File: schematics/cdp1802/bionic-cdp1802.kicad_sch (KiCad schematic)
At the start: 5 parts, among them J1 Bionic-P135, J2 Bionic-P245, U1 CDP1802, U2 74HCT126

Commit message: [CDP1802] Move schematics directory
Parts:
- added U3: 11AA010-I/TO, TO-92_MC_MCH, symbol 0-LocalLibrary:11AA010-I_TO
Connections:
- net GND: now also U3.1 (VSS)
- net VCC: now also U3.3 (VCC)
- net at J2.26 (P57): now also U3.2 (SCIO)
- no-connect marks 9 -> 8
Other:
- title: BionicCDP1802 Mezzanine -> BionicCDP1802

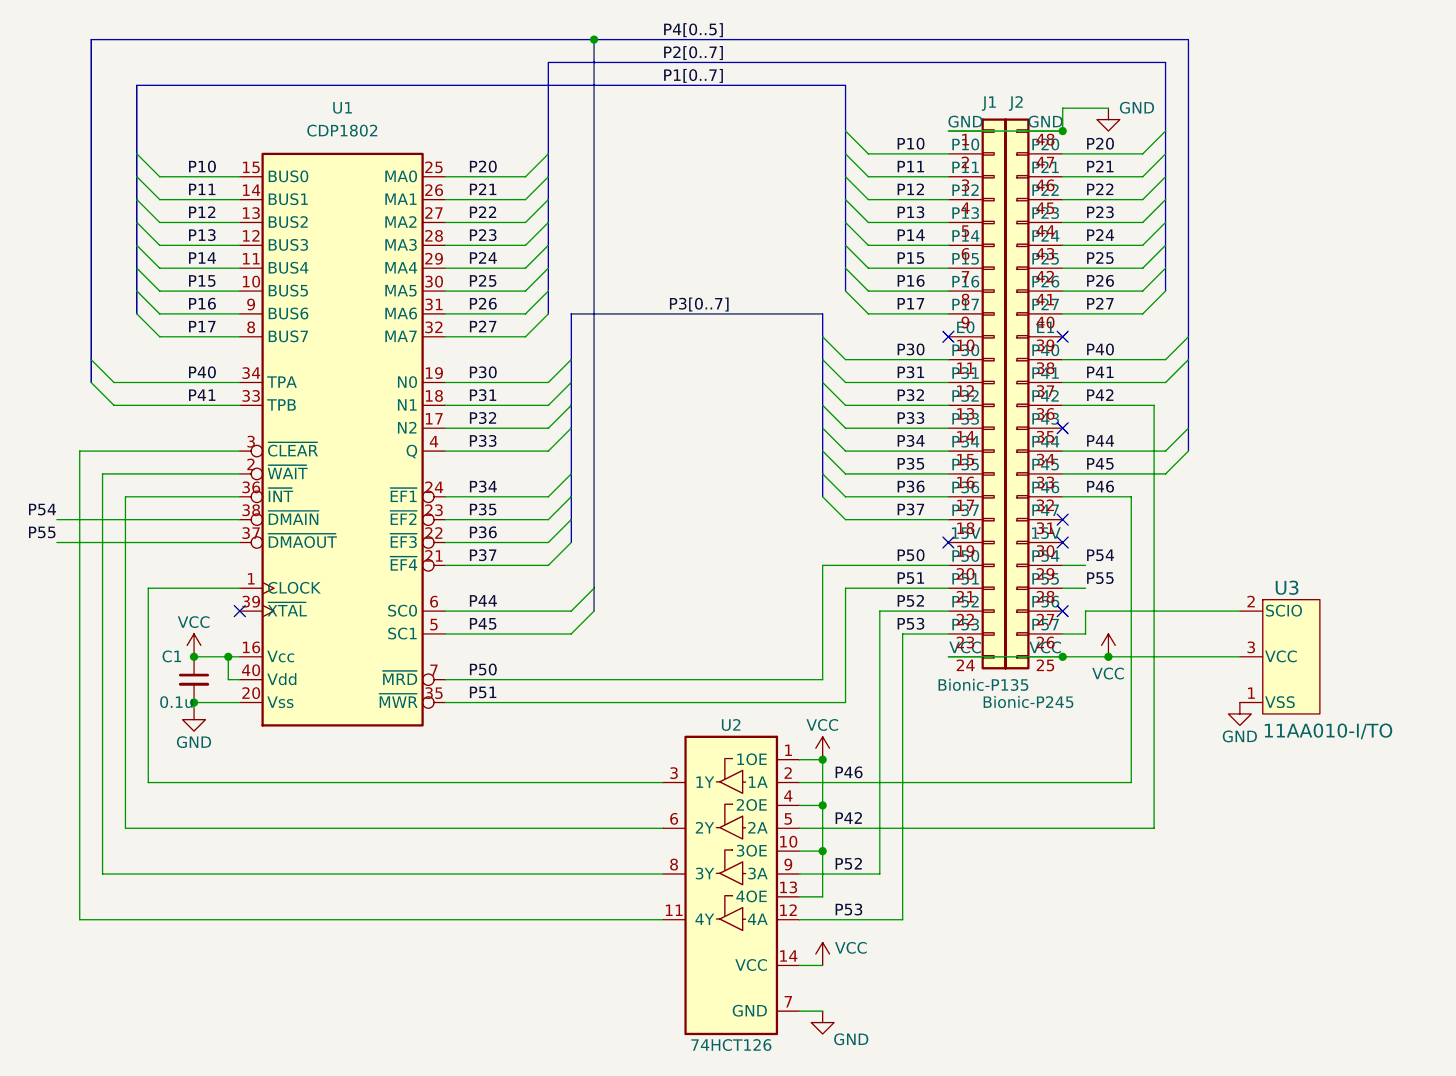
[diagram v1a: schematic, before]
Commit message: [CDP1802] Remove HC126
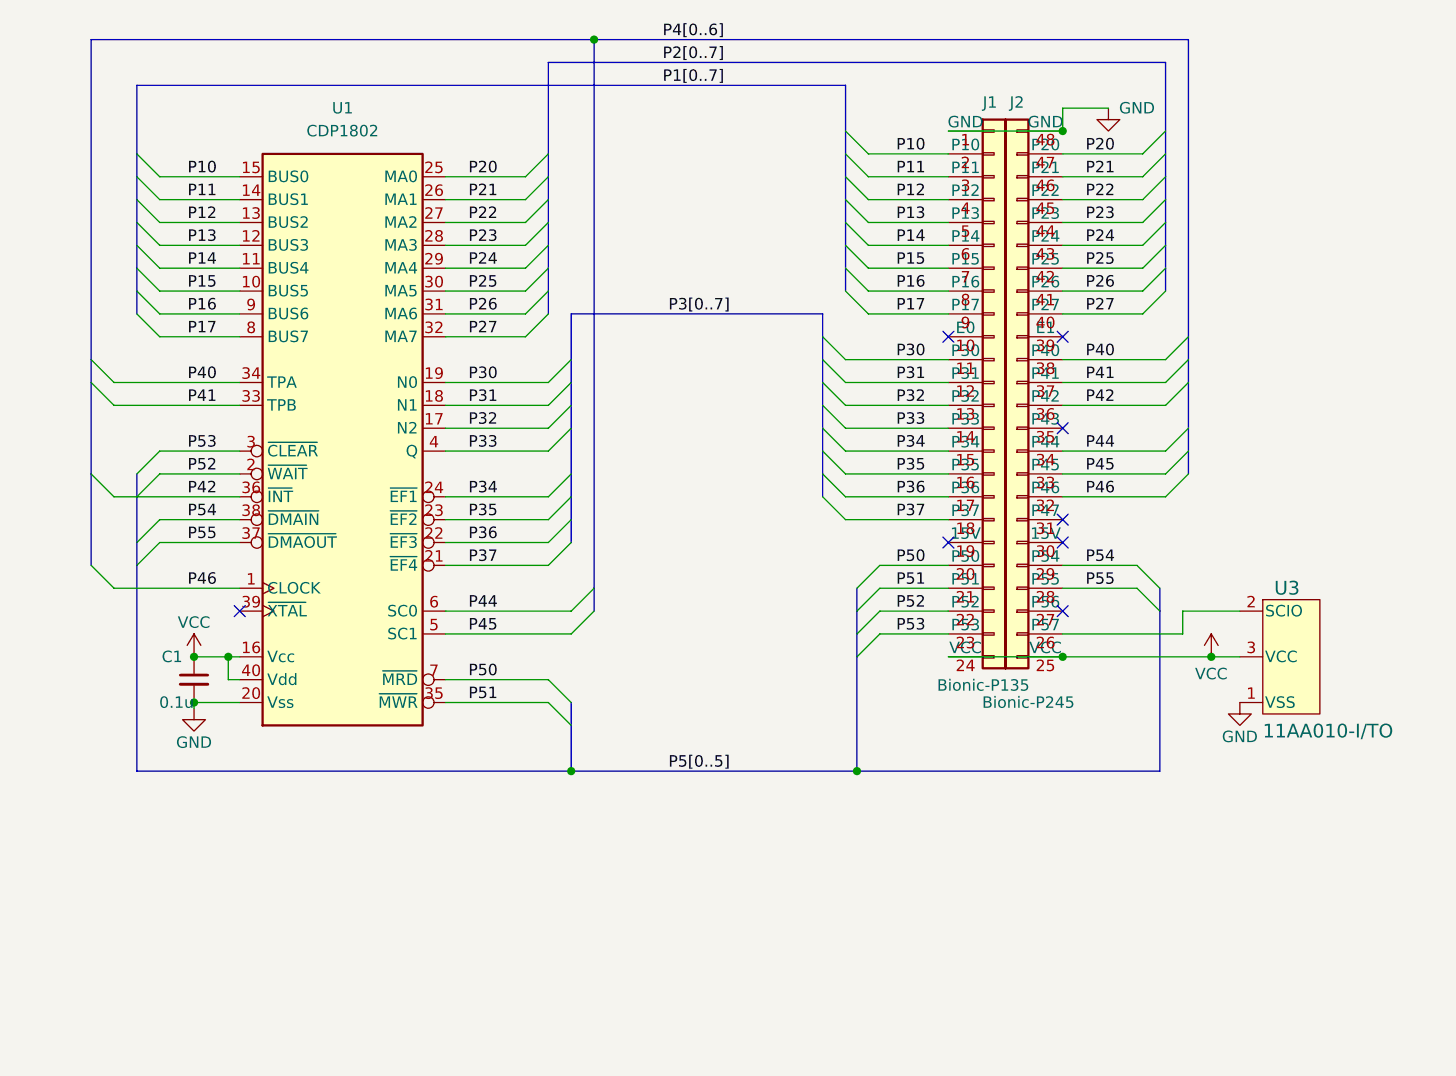
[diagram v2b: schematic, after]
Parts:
- removed U2: 74HCT126, Package_DIP:DIP-14_W7.62mm, symbol 0-LocalLibrary:74HCT126
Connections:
- net P42: now also U1.36 (~{INT})
- net P46: now also U1.1 (CLOCK)
- net P52: now also U1.2 (~{WAIT})
- net P53: now also U1.3 (~{CLEAR})
